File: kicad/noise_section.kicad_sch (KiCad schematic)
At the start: 50 parts, among them Q13 BC546, Q14 2N3904, U2 LM7805_TO220, U7 40106, U8 TL074

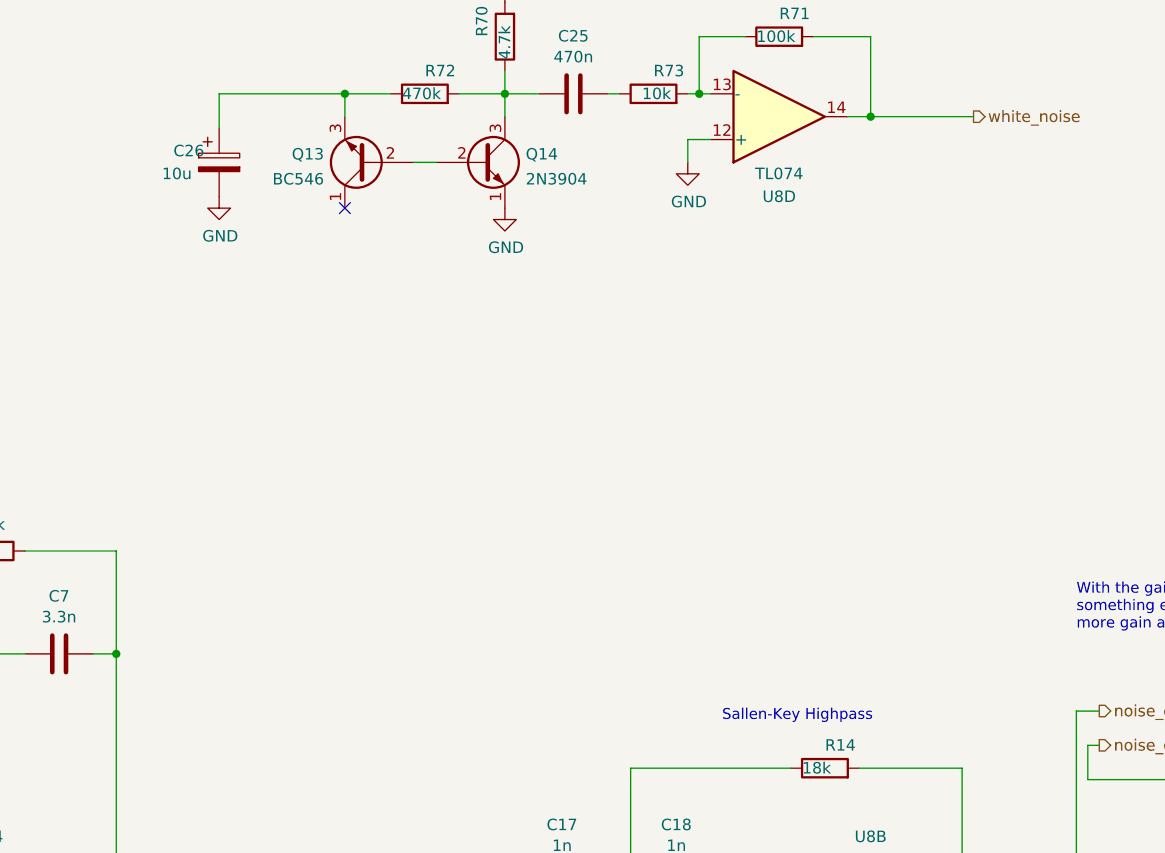
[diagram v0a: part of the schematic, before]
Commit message: fix noise section (1uF instead of 10uF), location of switch jacks!!, add resistor to make sizzle pot log-like and add note to use socket for cap to adjust tight decay
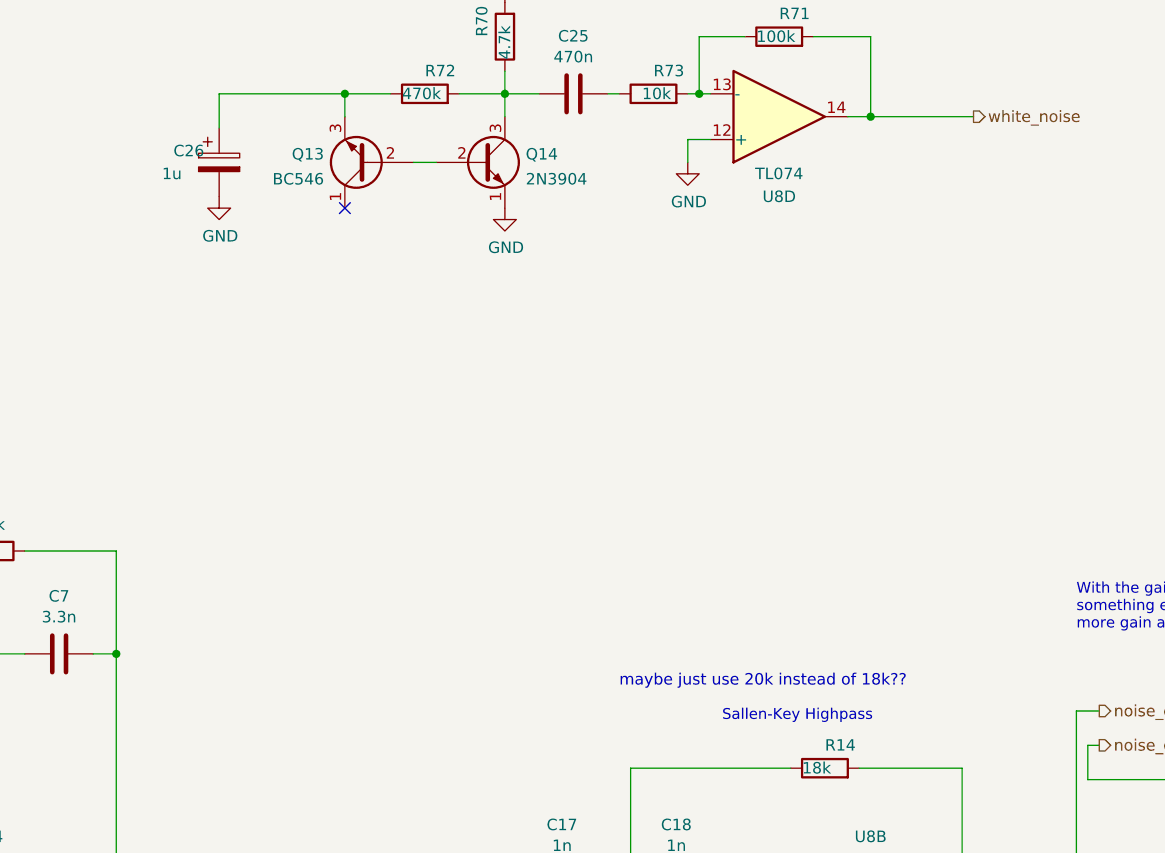
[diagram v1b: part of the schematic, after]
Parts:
- C26: value 10u -> 1u
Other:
- note added: "maybe just use 20k instead of 18k??"

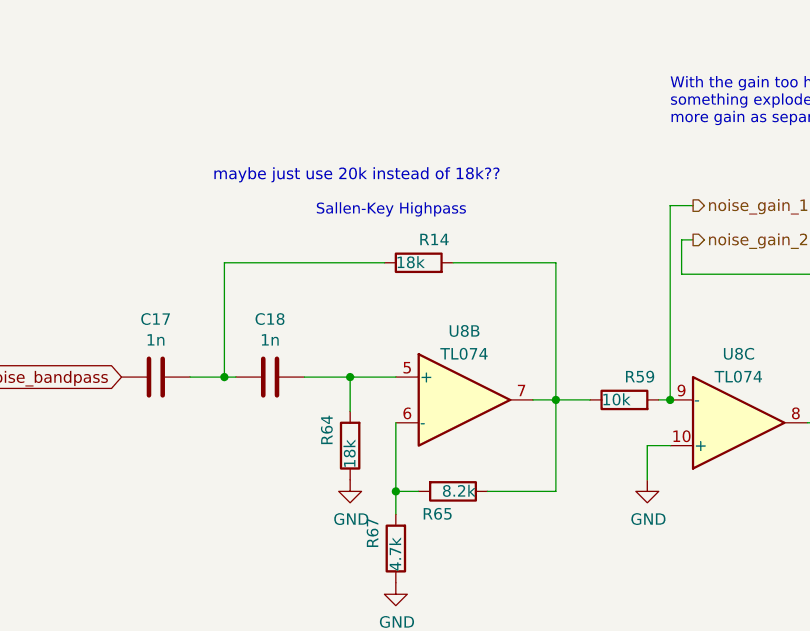
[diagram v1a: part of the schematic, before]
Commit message: change resistors in filter 18k to 20k
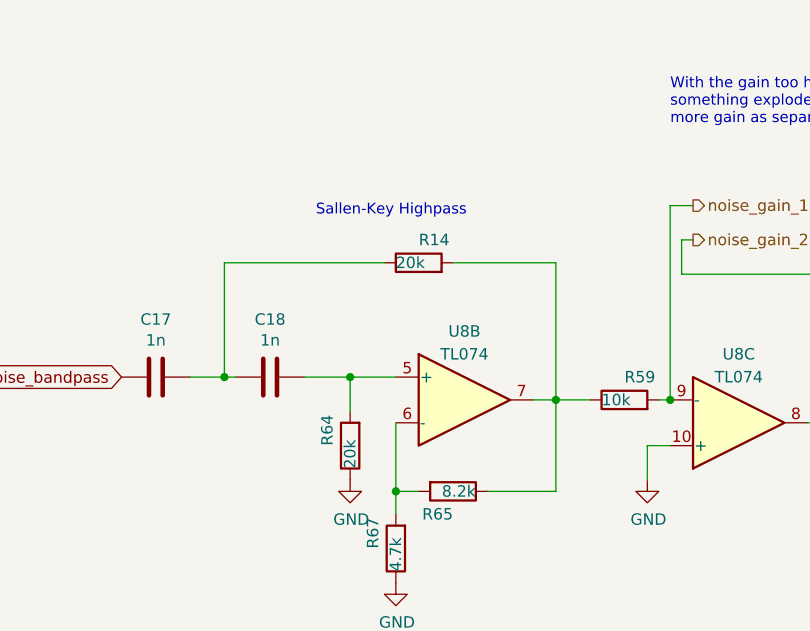
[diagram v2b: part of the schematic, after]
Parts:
- R14, R64: value 18k -> 20k
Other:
- note removed: "maybe just use 20k instead of 18k??"
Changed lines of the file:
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@@
     (effects (font (size 1.2 1.2)) (justify left bottom))
-  )
-  (text "maybe just use 20k instead of 18k??" (at 176.53 104.14 0)
-    (effects (font (size 1.27 1.27)) (justify left bottom))
   )
   (text "this should give noise around 6V peak2peak\nadjust R_feedback if not"
@@
       (effects (font (size 1.27 1.27)) (justify right))
     )
-    (property "Value" "18k" (id 1) (at 191.77 135.89 90)
+    (property "Value" "20k" (id 1) (at 191.77 135.89 90)
       (effects (font (size 1.27 1.27)) (justify right))
     )
@@
       (effects (font (size 1.27 1.27)) (justify right))
     )
-    (property "Value" "18k" (id 1) (at 196.85 113.03 90)
-      (effects (font (size 1.27 1.27)) (justify right))
-    )
+    (property "Value" "20k" (id 1) (at 196.85 113.03 90)
+      (effects (font (size 1.27 1.27)) (justify right))
+    )
